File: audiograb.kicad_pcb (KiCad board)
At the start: 2 copper layers, 0 parts

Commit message: add cm footprint
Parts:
- added U1: CM5108032, CM5108032:MODULE_CM5108032, F.Cu at (173.5, 75.5)

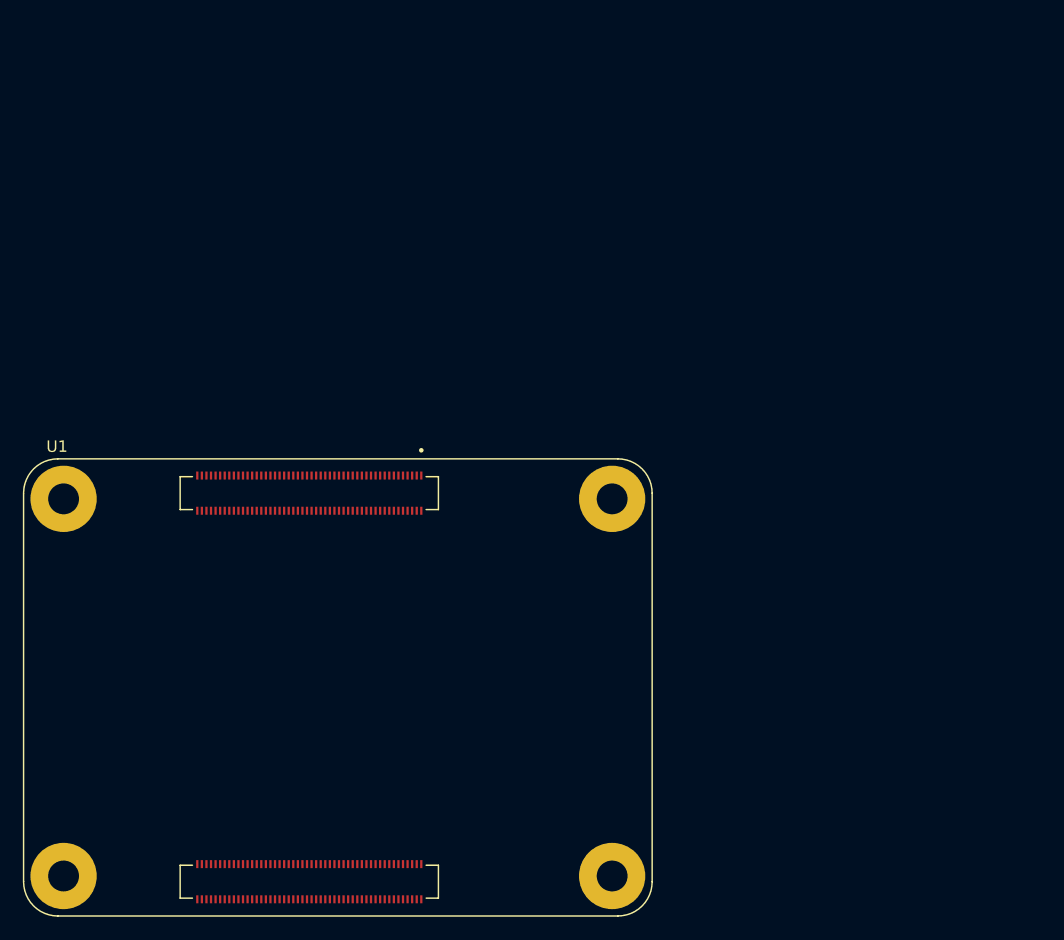
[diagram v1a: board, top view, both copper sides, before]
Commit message: add compute module header symbol and nets/pins
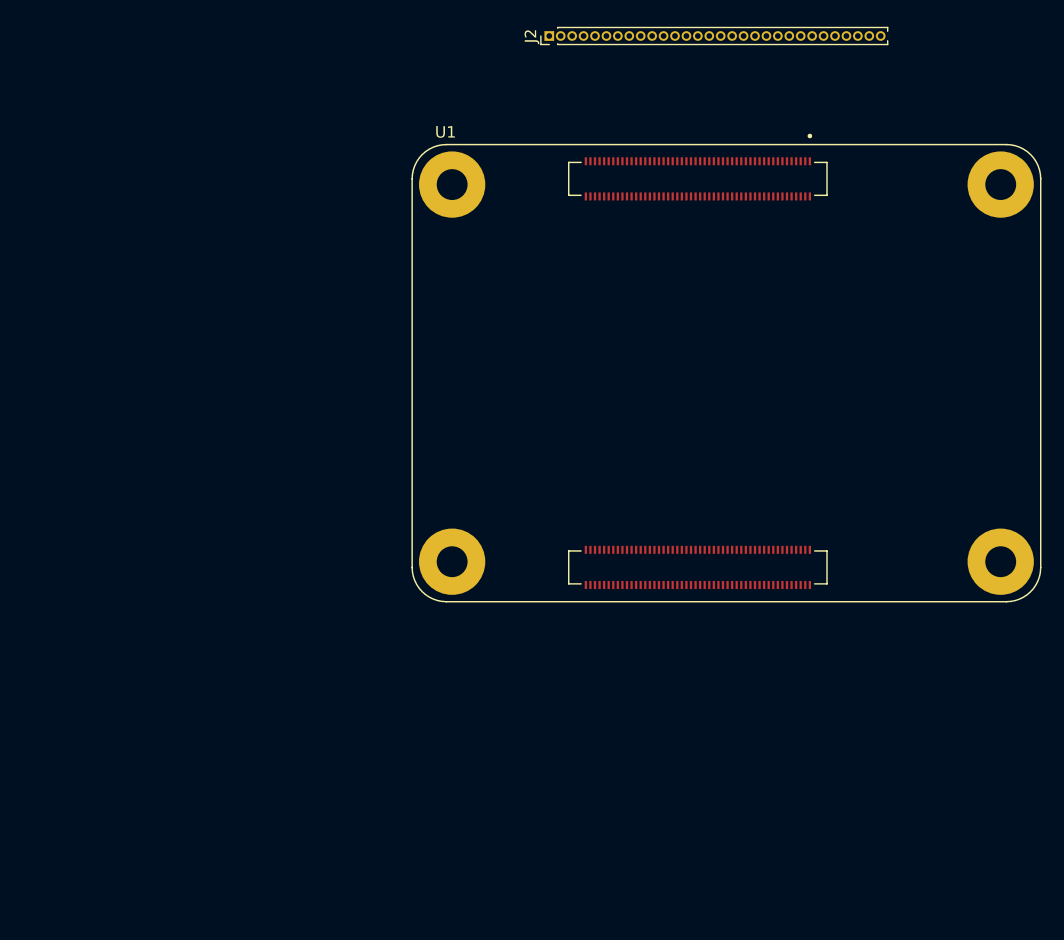
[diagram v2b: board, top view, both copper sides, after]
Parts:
- added J2: Conn_01x30, Connector_PinHeader_1.00mm:PinHeader_1x30_P1.00mm_Vertical, F.Cu at (192.0, 18.5)
- moved U1 43.7 mm to (207.5, 48.0)
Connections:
- U1 pad 24: unconnected-(U1A-GPIO26-Pad24) -> Net-(J2-Pin_26)
- U1 pad 25: unconnected-(U1A-GPIO21-Pad25) -> Net-(J2-Pin_21)
- U1 pad 26: unconnected-(U1A-GPIO19-Pad26) -> Net-(J2-Pin_19)
- U1 pad 27: unconnected-(U1A-GPIO20-Pad27) -> Net-(J2-Pin_20)
- U1 pad 28: unconnected-(U1A-GPIO13-Pad28) -> Net-(J2-Pin_13)
- U1 pad 29: unconnected-(U1A-GPIO16-Pad29) -> Net-(J2-Pin_16)
- U1 pad 30: unconnected-(U1A-GPIO6-Pad30) -> Net-(J2-Pin_6)
- U1 pad 31: unconnected-(U1A-GPIO12-Pad31) -> Net-(J2-Pin_12)
- U1 pad 34: unconnected-(U1A-GPIO5-Pad34) -> Net-(J2-Pin_5)
- U1 pad 37: unconnected-(U1A-GPIO7-Pad37) -> Net-(J2-Pin_7)
- U1 pad 38: unconnected-(U1A-GPIO11-Pad38) -> Net-(J2-Pin_11)
- U1 pad 39: unconnected-(U1A-GPIO8-Pad39) -> Net-(J2-Pin_8)
- U1 pad 40: unconnected-(U1A-GPIO9-Pad40) -> Net-(J2-Pin_9)
- U1 pad 41: unconnected-(U1A-GPIO25-Pad41) -> Net-(J2-Pin_25)
- U1 pad 44: unconnected-(U1A-GPIO10-Pad44) -> Net-(J2-Pin_10)
- U1 pad 45: unconnected-(U1A-GPIO24-Pad45) -> Net-(J2-Pin_24)
- U1 pad 46: unconnected-(U1A-GPIO22-Pad46) -> Net-(J2-Pin_22)
- U1 pad 47: unconnected-(U1A-GPIO23-Pad47) -> Net-(J2-Pin_23)
- U1 pad 48: unconnected-(U1A-GPIO27-Pad48) -> Net-(J2-Pin_27)
- U1 pad 49: unconnected-(U1A-GPIO18-Pad49) -> Net-(J2-Pin_18)
- U1 pad 50: unconnected-(U1A-GPIO17-Pad50) -> Net-(J2-Pin_17)
- U1 pad 51: unconnected-(U1A-GPIO15-Pad51) -> Net-(J2-Pin_15)
- U1 pad 54: unconnected-(U1A-GPIO4-Pad54) -> Net-(J2-Pin_4)
- U1 pad 55: unconnected-(U1A-GPIO14-Pad55) -> Net-(J2-Pin_14)
- U1 pad 56: unconnected-(U1A-GPIO3-Pad56) -> Net-(J2-Pin_3)
- U1 pad 58: unconnected-(U1A-GPIO2-Pad58) -> Net-(J2-Pin_2)

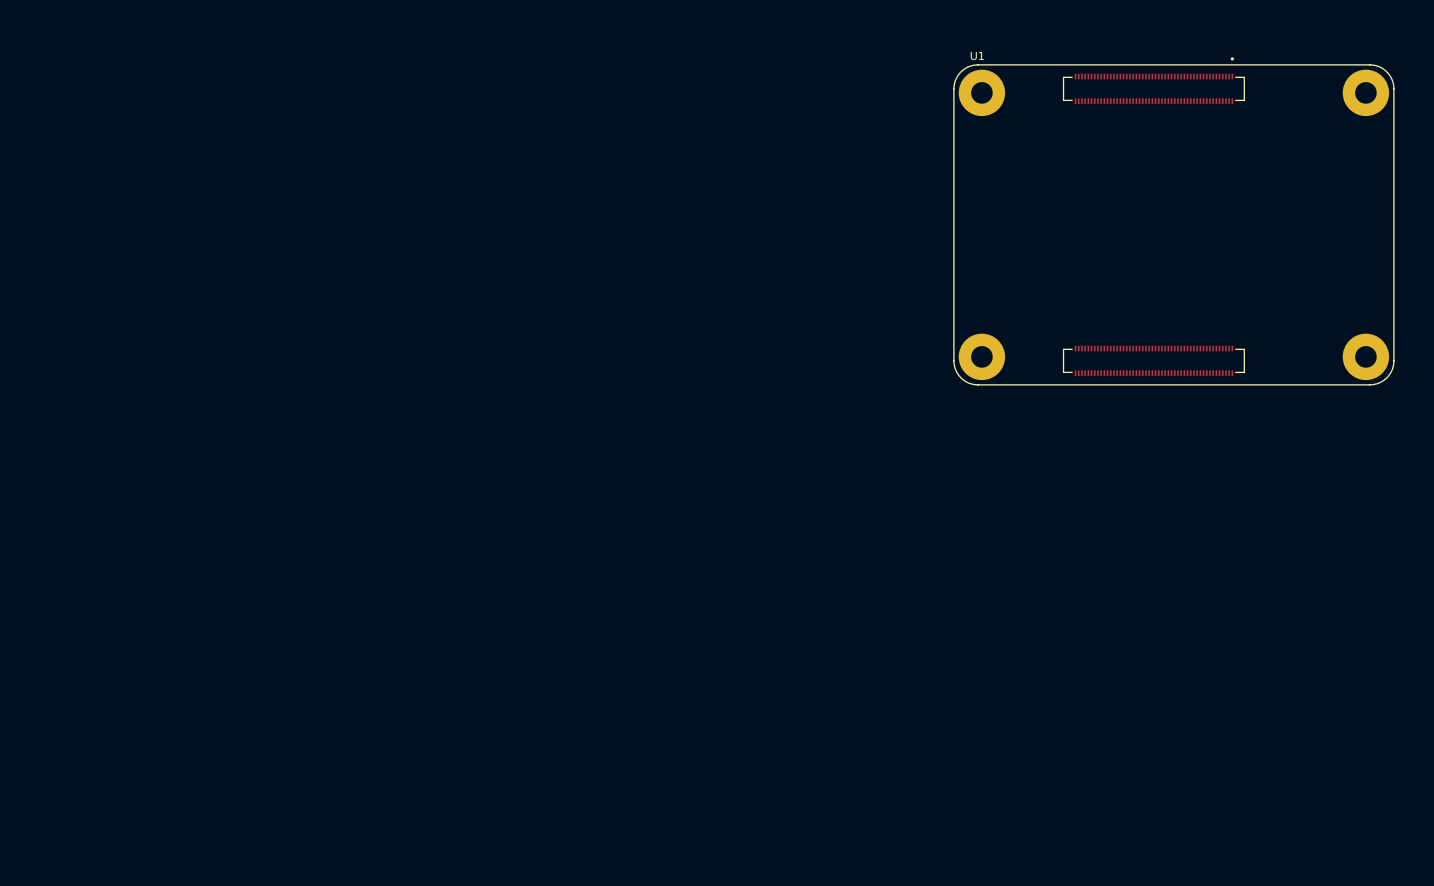
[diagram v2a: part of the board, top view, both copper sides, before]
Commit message: added more footprints and added to pcb
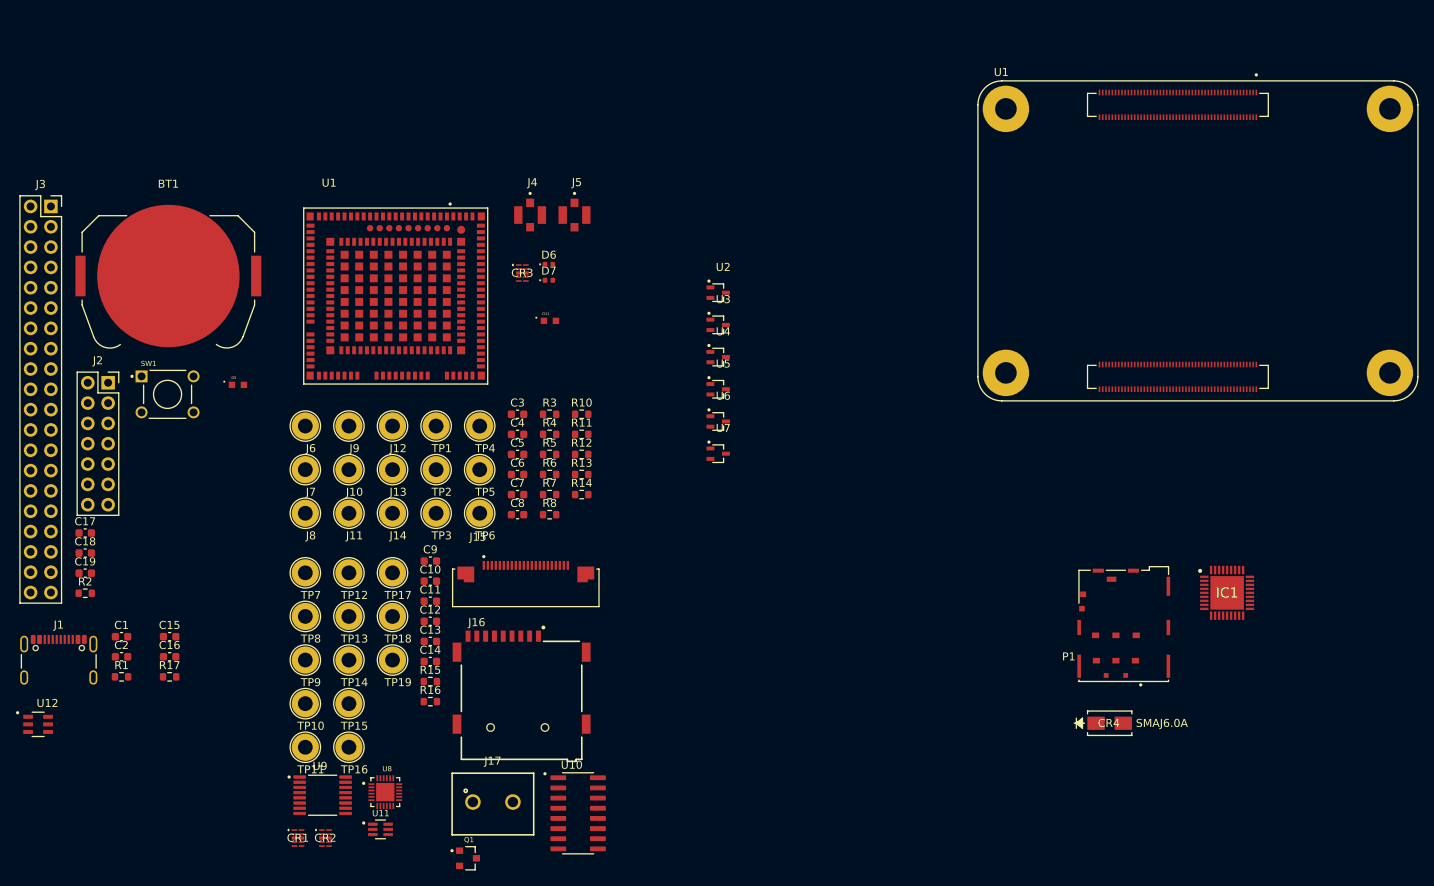
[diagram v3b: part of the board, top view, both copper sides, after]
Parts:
- added BT1: Battery_Cell, Battery:BatteryHolder_Keystone_3034_1x20mm, F.Cu at (81.8, 54.4)
- added C1: 100n, Capacitor_SMD:C_0603_1608Metric, F.Cu at (76.0, 99.5)
- added C10: 0.1uF, Capacitor_SMD:C_0603_1608Metric, F.Cu at (114.6, 92.5)
- added C11: 4.7uF, Capacitor_SMD:C_0603_1608Metric, F.Cu at (114.6, 95.0)
- added C12: 0.1uF, Capacitor_SMD:C_0603_1608Metric, F.Cu at (114.6, 97.6)
- added C13: 0.1uF ceramic, Capacitor_SMD:C_0603_1608Metric, F.Cu at (114.6, 100.1)
- added C14: 1uF, Capacitor_SMD:C_0603_1608Metric, F.Cu at (114.6, 102.6)
- added C15: 1.0 µ, Capacitor_SMD:C_0603_1608Metric, F.Cu at (82.0, 99.5)
- added C16: 1.0 µ, Capacitor_SMD:C_0603_1608Metric, F.Cu at (82.0, 102.0)
- added C17: 0.1uF ceramic, Capacitor_SMD:C_0603_1608Metric, F.Cu at (71.4, 86.5)
- added C18: 0.1uF, Capacitor_SMD:C_0603_1608Metric, F.Cu at (71.4, 89.0)
- added C19: 0.1uF, Capacitor_SMD:C_0603_1608Metric, F.Cu at (71.4, 91.5)
- added C2: 100n, Capacitor_SMD:C_0603_1608Metric, F.Cu at (76.0, 102.0)
- added C3: DNP 4.7nF, Capacitor_SMD:C_0603_1608Metric, F.Cu at (125.5, 71.7)
- added C4: 15pF, Capacitor_SMD:C_0603_1608Metric, F.Cu at (125.5, 74.2)
- added C5: 100nF, Capacitor_SMD:C_0603_1608Metric, F.Cu at (125.5, 76.7)
- added C6: 15uF, Capacitor_SMD:C_0603_1608Metric, F.Cu at (125.5, 79.2)
- added C7: 10nF, Capacitor_SMD:C_0603_1608Metric, F.Cu at (125.5, 81.7)
- added C8: 15uF, Capacitor_SMD:C_0603_1608Metric, F.Cu at (125.5, 84.2)
- added C9: 0.1uF ceramic, Capacitor_SMD:C_0603_1608Metric, F.Cu at (114.6, 90.0)
- added CR1: ESD7004MUTAG, ESD7004MUTAG:UDFN10_517BB_ONS, F.Cu at (98.0, 124.6)
- added CR2: ESD7004MUTAG, ESD7004MUTAG:UDFN10_517BB_ONS, F.Cu at (101.4, 124.6)
- added CR3: ESD7004MUTAG, ESD7004MUTAG:UDFN10_517BB_ONS, F.Cu at (126.1, 54.0)
- added CR4: SMAJ6.0A, SMAJ6.0A:SMASERIES_LTF, F.Cu at (199.5, 110.3)
- added D11: LED, LTST-C190GKT:LEDM1608X80, F.Cu at (129.5, 60.0)
- added D5: LED, LTST-C190GKT:LEDM1608X80, F.Cu at (90.5, 68.0)
- added D6: D_TVS, Diode_SMD:D_0402_1005Metric, F.Cu at (129.4, 52.9)
- added D7: D_TVS, Diode_SMD:D_0402_1005Metric, F.Cu at (129.4, 54.9)
- added IC1: USB2244I-AEZG-06, USB2244I-AEZG-06:QFN50P600X600X90-37N-D, F.Cu at (214.2, 94.0)
- added J1: USB_C_Receptacle_USB2.0_16P, Connector_USB:USB_C_Receptacle_GCT_USB4105-xx-A_16P_TopMnt_Horizontal, F.Cu at (68.1, 103.5)
- added J10: TestPoint, TestPoint:TestPoint_Loop_D2.50mm_Drill1.85mm, F.Cu at (104.4, 78.6)
- added J11: TestPoint, TestPoint:TestPoint_Loop_D2.50mm_Drill1.85mm, F.Cu at (104.4, 84.0)
- added J12: TestPoint, TestPoint:TestPoint_Loop_D2.50mm_Drill1.85mm, F.Cu at (109.8, 73.1)
- added J13: TestPoint, TestPoint:TestPoint_Loop_D2.50mm_Drill1.85mm, F.Cu at (109.8, 78.6)
- added J14: TestPoint, TestPoint:TestPoint_Loop_D2.50mm_Drill1.85mm, F.Cu at (109.8, 84.0)
- added J15: F32Q-1A7H1-11022, F32Q-1A7H1-11022:AMPHENOL_F32Q-1A7H1-11022, F.Cu at (126.5, 93.4)
- added J16: MEM2075-00-140-01-A, MEM2075-00-140-01-A:GCT_MEM2075-00-140-01-A, F.Cu at (125.5, 110.8)
- added J17: 691137710002, 691137710002:691137710002, F.Cu at (122.4, 120.1)
- added J2: SAM10346-ND, Connector_PinSocket_2.54mm:PinSocket_2x07_P2.54mm_Vertical, F.Cu at (74.3, 67.7)
- added J3: Conn_02x20_Odd_Even, Connector_PinSocket_2.54mm:PinSocket_2x20_P2.54mm_Vertical, F.Cu at (67.1, 45.7)
- added J4: CONMHF1-SMD-G-T, CONMHF1-SMD-G-T:LINX_CONMHF1-SMD-G-T, F.Cu at (127.0, 46.8)
- added J5: CONMHF1-SMD-G-T, CONMHF1-SMD-G-T:LINX_CONMHF1-SMD-G-T, F.Cu at (132.6, 46.8)
- added J6: TestPoint, TestPoint:TestPoint_Loop_D2.50mm_Drill1.85mm, F.Cu at (98.9, 73.1)
- added J7: TestPoint, TestPoint:TestPoint_Loop_D2.50mm_Drill1.85mm, F.Cu at (98.9, 78.6)
- added J8: TestPoint, TestPoint:TestPoint_Loop_D2.50mm_Drill1.85mm, F.Cu at (98.9, 84.0)
- added J9: TestPoint, TestPoint:TestPoint_Loop_D2.50mm_Drill1.85mm, F.Cu at (104.4, 73.1)
- added P1: SF72S006VBAR2500, SF72S006VBAR2500:JAE_SF72S006VBAR2500, F.Cu at (200.2, 97.9)
- added Q1: Q_PMOS_GSD, SSM3J358R_LF:TRANS_SSM3K333R_LF, F.Cu at (119.3, 127.2)
- added R1: 2.2k 1%, Resistor_SMD:R_0603_1608Metric, F.Cu at (76.0, 104.5)
- added R10: DNP 15k, Resistor_SMD:R_0603_1608Metric, F.Cu at (133.5, 71.7)
- added R11: 10k, Resistor_SMD:R_0603_1608Metric, F.Cu at (133.5, 74.2)
- added R12: 10k, Resistor_SMD:R_0603_1608Metric, F.Cu at (133.5, 76.7)
- added R13: 10k, Resistor_SMD:R_0603_1608Metric, F.Cu at (133.5, 79.2)
- added R14: 1k, Resistor_SMD:R_0603_1608Metric, F.Cu at (133.5, 81.7)
- added R15: 47k, Resistor_SMD:R_0603_1608Metric, F.Cu at (114.6, 105.1)
- added R16: 1k, Resistor_SMD:R_0603_1608Metric, F.Cu at (114.6, 107.6)
- added R17: 12.0 k, Resistor_SMD:R_0603_1608Metric, F.Cu at (82.0, 104.5)
- added R2: 1k, Resistor_SMD:R_0603_1608Metric, F.Cu at (71.4, 94.0)
- added R3: 10k, Resistor_SMD:R_0603_1608Metric, F.Cu at (129.5, 71.7)
- added R4: 10k, Resistor_SMD:R_0603_1608Metric, F.Cu at (129.5, 74.2)
- added R5: 10k, Resistor_SMD:R_0603_1608Metric, F.Cu at (129.5, 76.7)
- added R6: 10k, Resistor_SMD:R_0603_1608Metric, F.Cu at (129.5, 79.2)
- added R7: 10k, Resistor_SMD:R_0603_1608Metric, F.Cu at (129.5, 81.7)
- added R8: 10k, Resistor_SMD:R_0603_1608Metric, F.Cu at (129.5, 84.2)
- added SW1: 1825910-6, 1825910-6:SW_1825910-6-4, F.Cu at (81.7, 69.2)
- added TP1: T1, TestPoint:TestPoint_Loop_D2.50mm_Drill1.85mm, F.Cu at (115.3, 73.1)
- added TP10: TestPoint, TestPoint:TestPoint_Loop_D2.50mm_Drill1.85mm, F.Cu at (98.9, 107.8)
- added TP11: TestPoint, TestPoint:TestPoint_Loop_D2.50mm_Drill1.85mm, F.Cu at (98.9, 113.3)
- added TP12: TestPoint, TestPoint:TestPoint_Loop_D2.50mm_Drill1.85mm, F.Cu at (104.4, 91.5)
- added TP13: VDD_SD, TestPoint:TestPoint_Loop_D2.50mm_Drill1.85mm, F.Cu at (104.4, 96.9)
- added TP14: TestPoint, TestPoint:TestPoint_Loop_D2.50mm_Drill1.85mm, F.Cu at (104.4, 102.4)
- added TP15: TestPoint, TestPoint:TestPoint_Loop_D2.50mm_Drill1.85mm, F.Cu at (104.4, 107.8)
- added TP16: TestPoint, TestPoint:TestPoint_Loop_D2.50mm_Drill1.85mm, F.Cu at (104.4, 113.3)
- added TP17: Select, TestPoint:TestPoint_Loop_D2.50mm_Drill1.85mm, F.Cu at (109.8, 91.5)
- added TP18: TestPoint, TestPoint:TestPoint_Loop_D2.50mm_Drill1.85mm, F.Cu at (109.8, 96.9)
- added TP19: Enable, TestPoint:TestPoint_Loop_D2.50mm_Drill1.85mm, F.Cu at (109.8, 102.4)
- added TP2: T1, TestPoint:TestPoint_Loop_D2.50mm_Drill1.85mm, F.Cu at (115.3, 78.6)
- added TP3: T1, TestPoint:TestPoint_Loop_D2.50mm_Drill1.85mm, F.Cu at (115.3, 84.0)
- added TP4: T1, TestPoint:TestPoint_Loop_D2.50mm_Drill1.85mm, F.Cu at (120.7, 73.1)
- added TP5: T1, TestPoint:TestPoint_Loop_D2.50mm_Drill1.85mm, F.Cu at (120.7, 78.6)
- added TP6: T1, TestPoint:TestPoint_Loop_D2.50mm_Drill1.85mm, F.Cu at (120.7, 84.0)
- added TP7: TestPoint, TestPoint:TestPoint_Loop_D2.50mm_Drill1.85mm, F.Cu at (98.9, 91.5)
- added TP8: TestPoint, TestPoint:TestPoint_Loop_D2.50mm_Drill1.85mm, F.Cu at (98.9, 96.9)
- added TP9: TestPoint, TestPoint:TestPoint_Loop_D2.50mm_Drill1.85mm, F.Cu at (98.9, 102.4)
- added U1: RC7620_1104625, RC7620_1104625:XCVR_RC7620_1104625, F.Cu at (110.2, 56.9)
- added U10: CD4043BDR, CD4043BDR:SOIC127P600X175-16N, F.Cu at (133.0, 121.6)
- added U11: TPS22919DCKR, TPS22919DCKR:SOT65P210X110-6N, F.Cu at (108.3, 123.6)
- added U12: IP4220CZ6F, IP4220CZ6F:SOT95P275X110-6N, F.Cu at (65.5, 110.4)
- added U2: NX3008NBKW_115, NX3008NBKW_115:SOT65P210X110-3N, F.Cu at (150.5, 56.5)
- added U3: NX3008NBKW_115, NX3008NBKW_115:SOT65P210X110-3N, F.Cu at (150.5, 60.5)
- added U4: NX3008NBKW_115, NX3008NBKW_115:SOT65P210X110-3N, F.Cu at (150.5, 64.5)
- added U5: NX3008NBKW_115, NX3008NBKW_115:SOT65P210X110-3N, F.Cu at (150.5, 68.5)
- added U6: NX3008NBKW_115, NX3008NBKW_115:SOT65P210X110-3N, F.Cu at (150.5, 72.6)
- added U7: NX3008NBKW_115, NX3008NBKW_115:SOT65P210X110-3N, F.Cu at (150.5, 76.6)
- added U8: MAX4996LETG_, MAX4996ETG_:QFN40P350X350X80-25N, F.Cu at (108.9, 118.9)
- added U9: ~, SN74AVCH4T245PW:SOP65P640X120-16N, F.Cu at (101.1, 119.3)
- moved U1 3.61 mm to (210.5, 50.0)

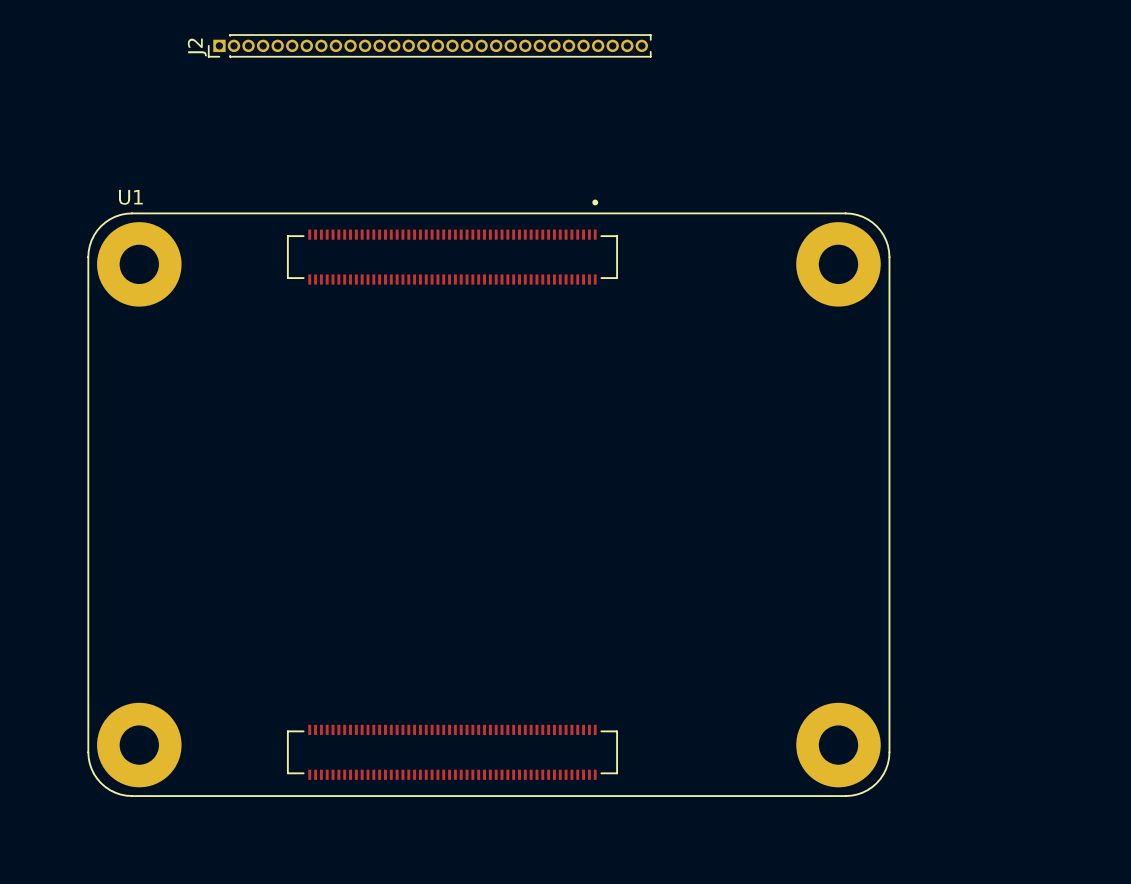
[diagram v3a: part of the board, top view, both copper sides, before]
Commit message: added components
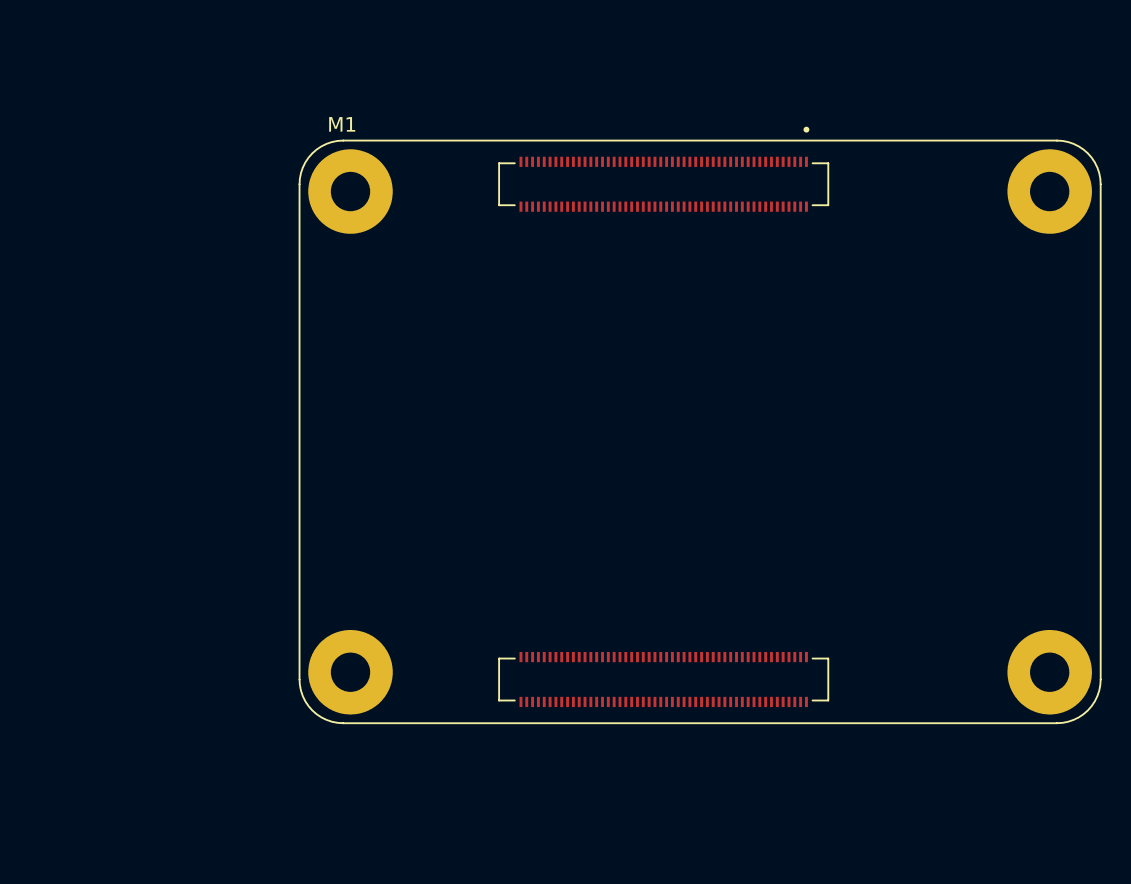
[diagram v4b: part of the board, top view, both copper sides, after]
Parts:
- removed the J2 at (192.0, 18.5)
- removed the U1 at (210.5, 50.0)
- added M1: ComputeModule5-CM5, CM5108032:MODULE_CM5108032, F.Cu at (225.0, 45.0)
